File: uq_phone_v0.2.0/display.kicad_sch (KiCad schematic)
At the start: 7 parts, among them U16 MCP1664T-E/OT

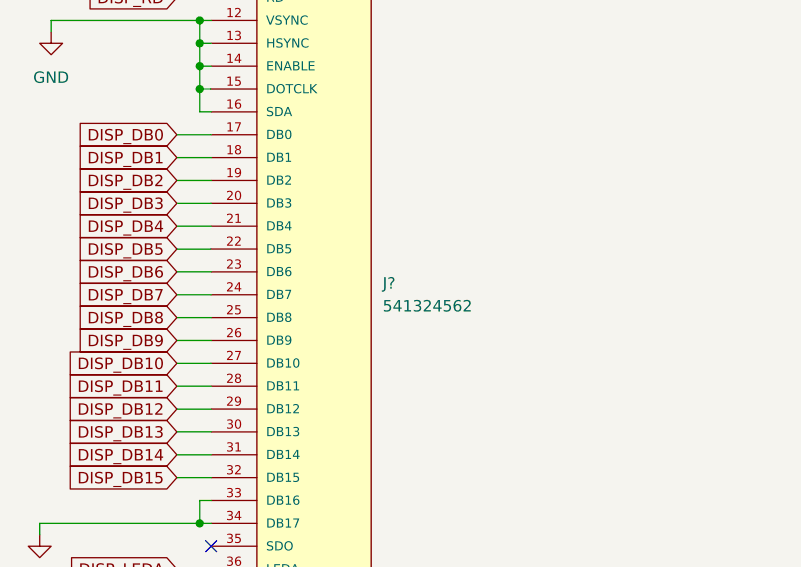
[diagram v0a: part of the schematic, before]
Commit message: Save PCB and schematic before STM32 FMC pin remapping
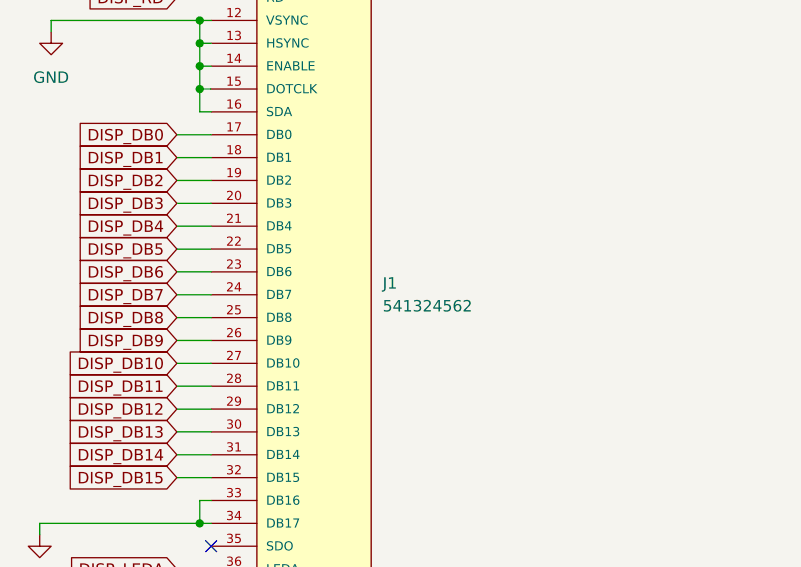
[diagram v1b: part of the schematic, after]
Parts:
- gave numbers to parts that had none: 1
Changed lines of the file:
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@@
 		(dnp no)
 		(fields_autoplaced yes)
-		(property "Reference" "J?"
+		(property "Reference" "J1"
 			(at 100.33 115.5699 0)
 			(effects
@@
 			(project "uq_phone"
 				(path "/14f57415-6807-40a5-bb38-3cb818a2cdae/ddca85db-d991-4949-b302-e774c1be11a1"
-					(reference "J?")
+					(reference "J1")
 					(unit 1)
 				)

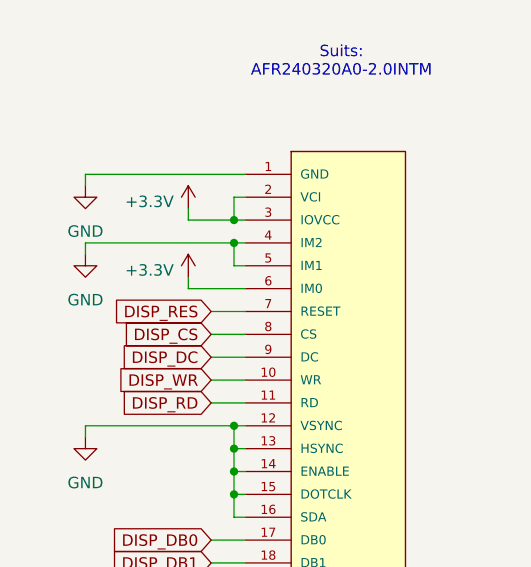
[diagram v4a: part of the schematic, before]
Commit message: Add GPIO expander and 16-bit FMC display schematic
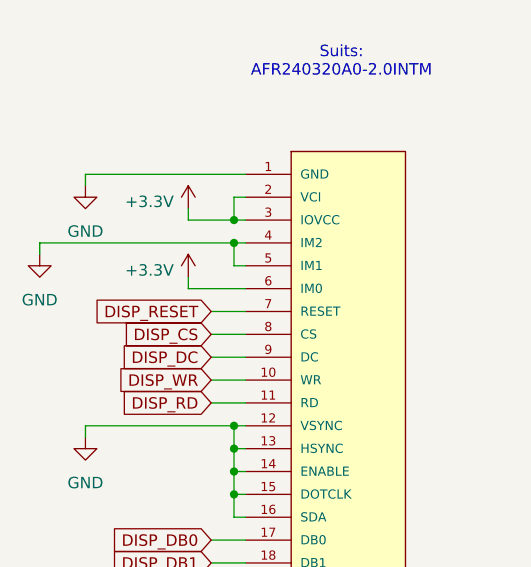
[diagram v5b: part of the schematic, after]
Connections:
- net DISP_RES renamed DISP_RESET
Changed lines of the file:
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@@
 	(wire
 		(pts
-			(xy 63.5 66.04) (xy 80.01 66.04)
+			(xy 58.42 66.04) (xy 80.01 66.04)
 		)
 		(stroke
@@
 	(wire
 		(pts
-			(xy 63.5 66.04) (xy 63.5 67.31)
+			(xy 58.42 66.04) (xy 58.42 67.31)
 		)
 		(stroke
@@
 		)
 	)
-	(global_label "DISP_RES"
+	(global_label "DISP_RESET"
 		(shape input)
 		(at 77.47 73.66 180)
@@
 		)
 		(property "Intersheetrefs" "${INTERSHEET_REFS}"
-			(at 65.5344 73.66 0)
+			(at 63.4178 73.66 0)
 			(effects
 				(font
@@
 		(instances
 			(project "uq_phone"
-				(path "/14f57415-6807-40a5-bb38-3cb818a2cdae/ddca85db-d991-4949-b302-e774c1be11a1"
+				(path "/14f57415-6807-40a5-bb38-3cb818a2cdae/626748c8-7389-49eb-8e46-a60885fec889"
 					(reference "#PWR083")
 					(unit 1)
@@
 		(instances
 			(project "uq_phone"
-				(path "/14f57415-6807-40a5-bb38-3cb818a2cdae/ddca85db-d991-4949-b302-e774c1be11a1"
+				(path "/14f57415-6807-40a5-bb38-3cb818a2cdae/626748c8-7389-49eb-8e46-a60885fec889"
 					(reference "C24")
 					(unit 1)
@@
 		(instances
 			(project "uq_phone"
-				(path "/14f57415-6807-40a5-bb38-3cb818a2cdae/ddca85db-d991-4949-b302-e774c1be11a1"
+				(path "/14f57415-6807-40a5-bb38-3cb818a2cdae/626748c8-7389-49eb-8e46-a60885fec889"
 					(reference "L2")
 					(unit 1)
@@
 		(instances
 			(project "uq_phone"
-				(path "/14f57415-6807-40a5-bb38-3cb818a2cdae/ddca85db-d991-4949-b302-e774c1be11a1"
+				(path "/14f57415-6807-40a5-bb38-3cb818a2cdae/626748c8-7389-49eb-8e46-a60885fec889"
 					(reference "#PWR0188")
 					(unit 1)
@@
 		(instances
 			(project "uq_phone"
-				(path "/14f57415-6807-40a5-bb38-3cb818a2cdae/ddca85db-d991-4949-b302-e774c1be11a1"
+				(path "/14f57415-6807-40a5-bb38-3cb818a2cdae/626748c8-7389-49eb-8e46-a60885fec889"
 					(reference "#PWR0227")
 					(unit 1)
@@
 		(instances
 			(project "uq_phone"
-				(path "/14f57415-6807-40a5-bb38-3cb818a2cdae/ddca85db-d991-4949-b302-e774c1be11a1"
+				(path "/14f57415-6807-40a5-bb38-3cb818a2cdae/626748c8-7389-49eb-8e46-a60885fec889"
 					(reference "#PWR065")
 					(unit 1)
@@
 	(symbol
 		(lib_id "power:GND")
-		(at 63.5 67.31 0)
+		(at 58.42 67.31 0)
 		(unit 1)
 		(exclude_from_sim no)
@@
 		(fields_autoplaced yes)
 		(property "Reference" "#PWR081"
-			(at 63.5 73.66 0)
+			(at 58.42 73.66 0)
 			(effects
 				(font
@@
 		)
 		(property "Value" "GND"
-			(at 63.5 72.39 0)
+			(at 58.42 72.39 0)
 			(effects
 				(font
@@
 		)
 		(property "Footprint" ""
-			(at 63.5 67.31 0)
+			(at 58.42 67.31 0)
 			(effects
 				(font
@@
 		)
 		(property "Datasheet" ""
-			(at 63.5 67.31 0)
+			(at 58.42 67.31 0)
 			(effects
 				(font
@@
 		)
 		(property "Description" "Power symbol creates a global label with name \"GND\" , ground"
-			(at 63.5 67.31 0)
+			(at 58.42 67.31 0)
 			(effects
 				(font
@@
 		(instances
 			(project "uq_phone"
-				(path "/14f57415-6807-40a5-bb38-3cb818a2cdae/ddca85db-d991-4949-b302-e774c1be11a1"
+				(path "/14f57415-6807-40a5-bb38-3cb818a2cdae/626748c8-7389-49eb-8e46-a60885fec889"
 					(reference "#PWR081")
 					(unit 1)
@@
 		(instances
 			(project "uq_phone"
-				(path "/14f57415-6807-40a5-bb38-3cb818a2cdae/ddca85db-d991-4949-b302-e774c1be11a1"
+				(path "/14f57415-6807-40a5-bb38-3cb818a2cdae/626748c8-7389-49eb-8e46-a60885fec889"
 					(reference "D13")
 					(unit 1)
@@
 		(instances
 			(project "uq_phone"
-				(path "/14f57415-6807-40a5-bb38-3cb818a2cdae/ddca85db-d991-4949-b302-e774c1be11a1"
+				(path "/14f57415-6807-40a5-bb38-3cb818a2cdae/626748c8-7389-49eb-8e46-a60885fec889"
 					(reference "#PWR0169")
 					(unit 1)
@@
 		(instances
 			(project "uq_phone"
-				(path "/14f57415-6807-40a5-bb38-3cb818a2cdae/ddca85db-d991-4949-b302-e774c1be11a1"
+				(path "/14f57415-6807-40a5-bb38-3cb818a2cdae/626748c8-7389-49eb-8e46-a60885fec889"
 					(reference "C61")
 					(unit 1)
@@
 		(instances
 			(project "uq_phone"
-				(path "/14f57415-6807-40a5-bb38-3cb818a2cdae/ddca85db-d991-4949-b302-e774c1be11a1"
+				(path "/14f57415-6807-40a5-bb38-3cb818a2cdae/626748c8-7389-49eb-8e46-a60885fec889"
 					(reference "U16")
 					(unit 1)
@@
 		(instances
 			(project "uq_phone"
-				(path "/14f57415-6807-40a5-bb38-3cb818a2cdae/ddca85db-d991-4949-b302-e774c1be11a1"
+				(path "/14f57415-6807-40a5-bb38-3cb818a2cdae/626748c8-7389-49eb-8e46-a60885fec889"
 					(reference "#PWR0161")
 					(unit 1)
@@
 		(instances
 			(project "uq_phone"
-				(path "/14f57415-6807-40a5-bb38-3cb818a2cdae/ddca85db-d991-4949-b302-e774c1be11a1"
+				(path "/14f57415-6807-40a5-bb38-3cb818a2cdae/626748c8-7389-49eb-8e46-a60885fec889"
 					(reference "J1")
 					(unit 1)
@@
 		(instances
 			(project "uq_phone"
-				(path "/14f57415-6807-40a5-bb38-3cb818a2cdae/ddca85db-d991-4949-b302-e774c1be11a1"
+				(path "/14f57415-6807-40a5-bb38-3cb818a2cdae/626748c8-7389-49eb-8e46-a60885fec889"
 					(reference "#PWR0172")
 					(unit 1)
@@
 		(instances
 			(project "uq_phone"
-				(path "/14f57415-6807-40a5-bb38-3cb818a2cdae/ddca85db-d991-4949-b302-e774c1be11a1"
+				(path "/14f57415-6807-40a5-bb38-3cb818a2cdae/626748c8-7389-49eb-8e46-a60885fec889"
 					(reference "#PWR0226")
 					(unit 1)
@@
 		(instances
 			(project "uq_phone"
-				(path "/14f57415-6807-40a5-bb38-3cb818a2cdae/ddca85db-d991-4949-b302-e774c1be11a1"
+				(path "/14f57415-6807-40a5-bb38-3cb818a2cdae/626748c8-7389-49eb-8e46-a60885fec889"
 					(reference "#PWR0225")
 					(unit 1)
@@
 		(instances
 			(project "uq_phone"
-				(path "/14f57415-6807-40a5-bb38-3cb818a2cdae/ddca85db-d991-4949-b302-e774c1be11a1"
+				(path "/14f57415-6807-40a5-bb38-3cb818a2cdae/626748c8-7389-49eb-8e46-a60885fec889"
 					(reference "#PWR092")
 					(unit 1)
@@
 		(instances
 			(project "uq_phone"
-				(path "/14f57415-6807-40a5-bb38-3cb818a2cdae/ddca85db-d991-4949-b302-e774c1be11a1"
+				(path "/14f57415-6807-40a5-bb38-3cb818a2cdae/626748c8-7389-49eb-8e46-a60885fec889"
 					(reference "R32")
 					(unit 1)
@@
 		(instances
 			(project "uq_phone"
-				(path "/14f57415-6807-40a5-bb38-3cb818a2cdae/ddca85db-d991-4949-b302-e774c1be11a1"
+				(path "/14f57415-6807-40a5-bb38-3cb818a2cdae/626748c8-7389-49eb-8e46-a60885fec889"
 					(reference "#PWR0143")
 					(unit 1)
